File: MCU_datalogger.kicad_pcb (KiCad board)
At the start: 2 copper layers, 29 parts, among them J1 Conn_01x04_Pin, J2 Conn_01x04_Pin, J3 Conn_01x09_Pin, J4 Conn_02x03_Odd_Even, U1 24LC1025, U2 24LC1025, U3 DS1337S_, U4 ATMEGA328P-AU, Y1 32.768 KHz, Y2 16 MHz

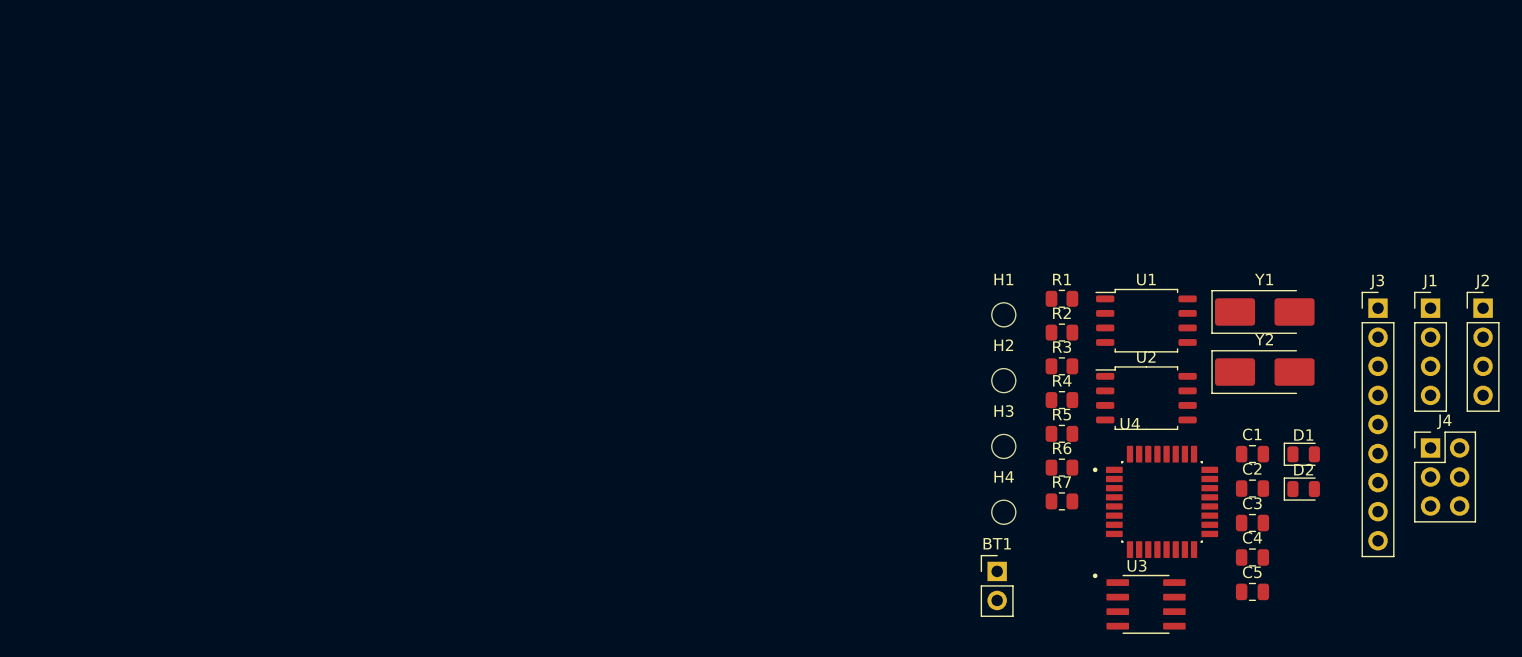
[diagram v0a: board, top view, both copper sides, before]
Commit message: placed footprints in layout
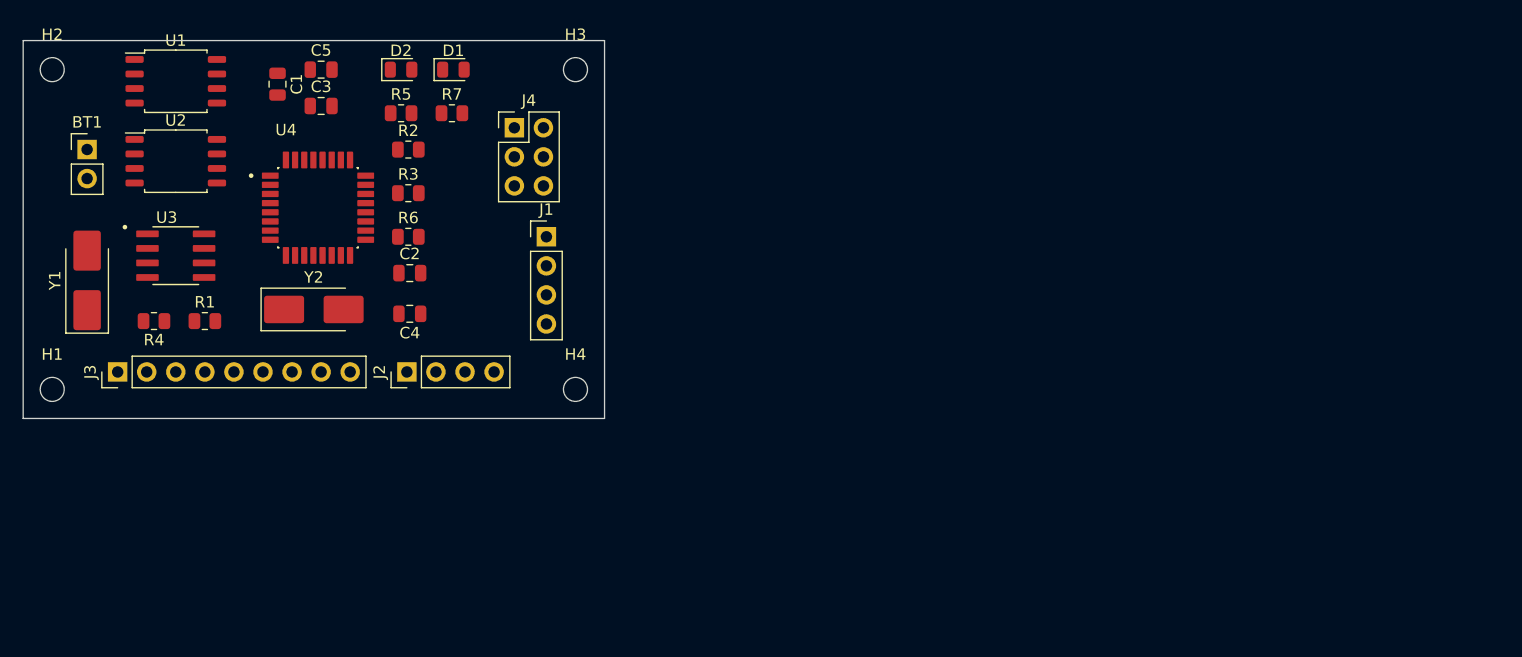
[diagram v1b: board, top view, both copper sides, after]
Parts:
- moved J3 110.3 mm to (46.4, 92.5), turned to 90 degrees
- moved Y1 102.9 mm to (43.7, 84.5), turned to 90 degrees
- moved J2 94.2 mm to (71.6, 92.5), turned to 90 degrees
- moved C5 93.3 mm to (64.1, 66.0)
- moved C1 91.1 mm to (60.3, 67.3), turned to -90 degrees
- moved U3 90.1 mm to (51.4, 82.3)
- moved C3 89.2 mm to (64.1, 69.2)
- moved BT1 87.6 mm to (43.7, 73.0)
- moved H2 87.5 mm to (40.6, 66.0)
- moved U1 87.4 mm to (51.4, 67.1)
- moved U2 87.3 mm to (51.4, 74.0)
- moved D2 87.0 mm to (71.1, 66.0)
- moved J4 84.8 mm to (81.0, 71.1)
- moved H1 83.4 mm to (40.6, 94.0)
- moved Y2 83.3 mm to (63.5, 87.0)
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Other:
- board outline added: 50.8 x 33 mm

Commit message: routing complete
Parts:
- moved R1 24.3 mm to (77.0, 80.3), turned to 180 degrees
- moved R6 19.2 mm to (53.6, 86.9), turned to 180 degrees
- moved R2 7.24 mm to (71.9, 80.3), turned to 180 degrees
- moved R5 6.49 mm to (76.7, 73.2), turned to 180 degrees
- moved D2 6.14 mm to (76.7, 68.6)
- moved R7 4.95 mm to (71.9, 73.2)
- moved D1 4.58 mm to (71.9, 68.6)
- moved R4 1.17 mm to (49.3, 86.9), turned to 0 degrees
- moved Y2 0.51 mm to (63.0, 87.0)
- moved C2 0.25 mm to (71.9, 84.1), turned to 180 degrees
- moved R3 0.13 mm to (71.9, 76.8), turned to 180 degrees
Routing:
- net VCC: track 0.00 -> 182.3 mm, vias 0 -> 5
- net /SCK: track 0.00 -> 101.2 mm, vias 0 -> 3
- net GND: track 0.00 -> 61.8 mm, vias 0 -> 4
- net /SDA: track 0.00 -> 57.1 mm, vias 0 -> 2
- net /CLK_16M_RTN: track 0.00 -> 33.0 mm, vias 0 -> 2
- net /TX: track 0.00 -> 29.6 mm, vias 0 -> 1
- net /RST_N: track 0.00 -> 29.5 mm, vias 0 -> 2
- net /RX: track 0.00 -> 28.0 mm, vias 0 -> 1
- net /D2: track 0.00 -> 26.2 mm, vias 0 -> 1
- net /MOSI: track 0.00 -> 26.2 mm
- net /D3: track 0.00 -> 25.9 mm
- net /CLK_16M: track 0.00 -> 25.1 mm
- net /D4: track 0.00 -> 23.1 mm
- net /MISO: track 0.00 -> 20.9 mm, vias 0 -> 1
- net /AREF: track 0.00 -> 15.1 mm, vias 0 -> 2
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
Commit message: added copper fills
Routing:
- net /CLK_16M_RTN: track 33.0 -> 28.4 mm
- added copper zone on B.Cu, net GND
- added copper zone on F.Cu, net VCC
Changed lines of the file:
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@@
 	)
 	(segment
-		(start 59.436 80.264)
-		(end 58.166 78.994)
+		(start 61.126273 76.2)
+		(end 61.966695 76.2)
+		(width 0.25)
+		(layer "B.Cu")
+		(net "/CLK_16M_RTN")
+	)
+	(segment
+		(start 60.643 76.683273)
+		(end 61.126273 76.2)
+		(width 0.25)
+		(layer "B.Cu")
+		(net "/CLK_16M_RTN")
+	)
+	(segment
+		(start 60.643 79.185)
+		(end 60.643 76.683273)
+		(width 0.25)
+		(layer "B.Cu")
+		(net "/CLK_16M_RTN")
+	)
+	(segment
+		(start 61.722 80.264)
+		(end 60.643 79.185)
+		(width 0.25)
+		(layer "B.Cu")
+		(net "/CLK_16M_RTN")
+	)
+	(segment
+		(start 65.278 72.898)
+		(end 65.278 71.12)
+		(width 0.25)
+		(layer "B.Cu")
+		(net "/CLK_16M_RTN")
+	)
+	(segment
+		(start 61.966695 76.2)
+		(end 65.268695 72.898)
 		(width 0.25)
 		(layer "B.Cu")
@@
 		(start 65.268695 72.898)
 		(end 65.278 72.898)
-		(width 0.25)
-		(layer "B.Cu")
-		(net "/CLK_16M_RTN")
-	)
-	(segment
-		(start 61.722 80.264)
-		(end 59.436 80.264)
-		(width 0.25)
-		(layer "B.Cu")
-		(net "/CLK_16M_RTN")
-	)
-	(segment
-		(start 65.278 72.898)
-		(end 65.278 71.12)
-		(width 0.25)
-		(layer "B.Cu")
-		(net "/CLK_16M_RTN")
-	)
-	(segment
-		(start 58.166 78.994)
-		(end 58.166 76.962)
-		(width 0.25)
-		(layer "B.Cu")
-		(net "/CLK_16M_RTN")
-	)
-	(segment
-		(start 58.166 76.962)
-		(end 58.928 76.2)
-		(width 0.25)
-		(layer "B.Cu")
-		(net "/CLK_16M_RTN")
-	)
-	(segment
-		(start 58.928 76.2)
-		(end 61.966695 76.2)
-		(width 0.25)
-		(layer "B.Cu")
-		(net "/CLK_16M_RTN")
-	)
-	(segment
-		(start 61.966695 76.2)
-		(end 65.268695 72.898)
 		(width 0.25)
 		(layer "B.Cu")
@@
 		(net "/LED1_OUT")
 	)
+	(zone
+		(net "VCC")
+		(layer "F.Cu")
+		(hatch edge 0.5)
+		(connect_pads
+			(clearance 0.5)
+		)
+		(min_thickness 0.25)
+		(fill yes
+			(thermal_gap 0.5)
+			(thermal_bridge_width 0.5)
+			(island_removal_mode 0)
+		)
+		(polygon
+			(pts
+				(xy 87.376 89.408) (xy 87.376 70.866) (xy 80.264 63.754) (xy 46.736 63.754) (xy 40.64 69.85) (xy 40.64 90.424)
+				(xy 45.466 95.25) (xy 81.534 95.25)
+			)
+		)
+	)
+	(zone
+		(net "GND")
+		(layer "B.Cu")
+		(hatch edge 0.5)
+		(connect_pads
+			(clearance 0.5)
+		)
+		(min_thickness 0.25)
+		(fill yes
+			(thermal_gap 0.5)
+			(thermal_bridge_width 0.5)
+			(island_removal_mode 0)
+		)
+		(polygon
+			(pts
+				(xy 87.376 89.408) (xy 87.376 70.866) (xy 80.264 63.754) (xy 46.736 63.754) (xy 40.64 69.85) (xy 40.64 90.424)
+				(xy 45.466 95.25) (xy 81.534 95.25)
+			)
+		)
+	)
 	(embedded_fonts no)
